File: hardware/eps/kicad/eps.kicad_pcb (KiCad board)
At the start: 2 copper layers, 96 x 90.2 mm, 85 parts, among them J1 B2B-PH-K-S(LF)(SN), J2 B2B-PH-K-S(LF)(SN), J3 B2B-PH-K-S(LF)(SN), J4 B2B-PH-K-S(LF)(SN), J5 B2B-PH-K-S(LF)(SN), J5 XT30PW-F, J6 B2B-PH-K-S(LF)(SN), J7 TSW-103-07-F-S, J8 68000-102HLF, J9 68000-102HLF, Q1 FDMC8327L, Q2 FDMC8327L, U1 LTC4162EUFD-LADMTRPBF, U2 TPS62933FDRLR, U3 TPS62933FDRLR

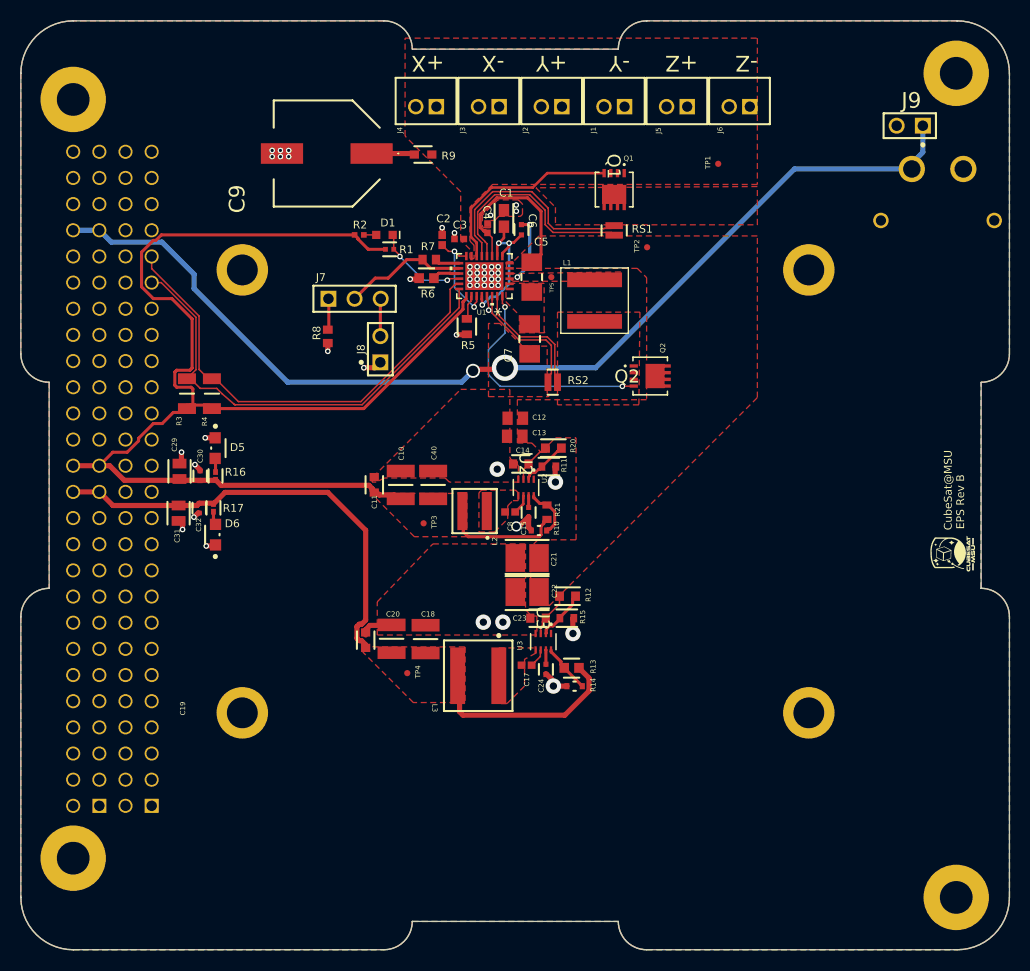
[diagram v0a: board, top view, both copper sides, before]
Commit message: attempt to convert altium to kicad, lost foot prints, not good
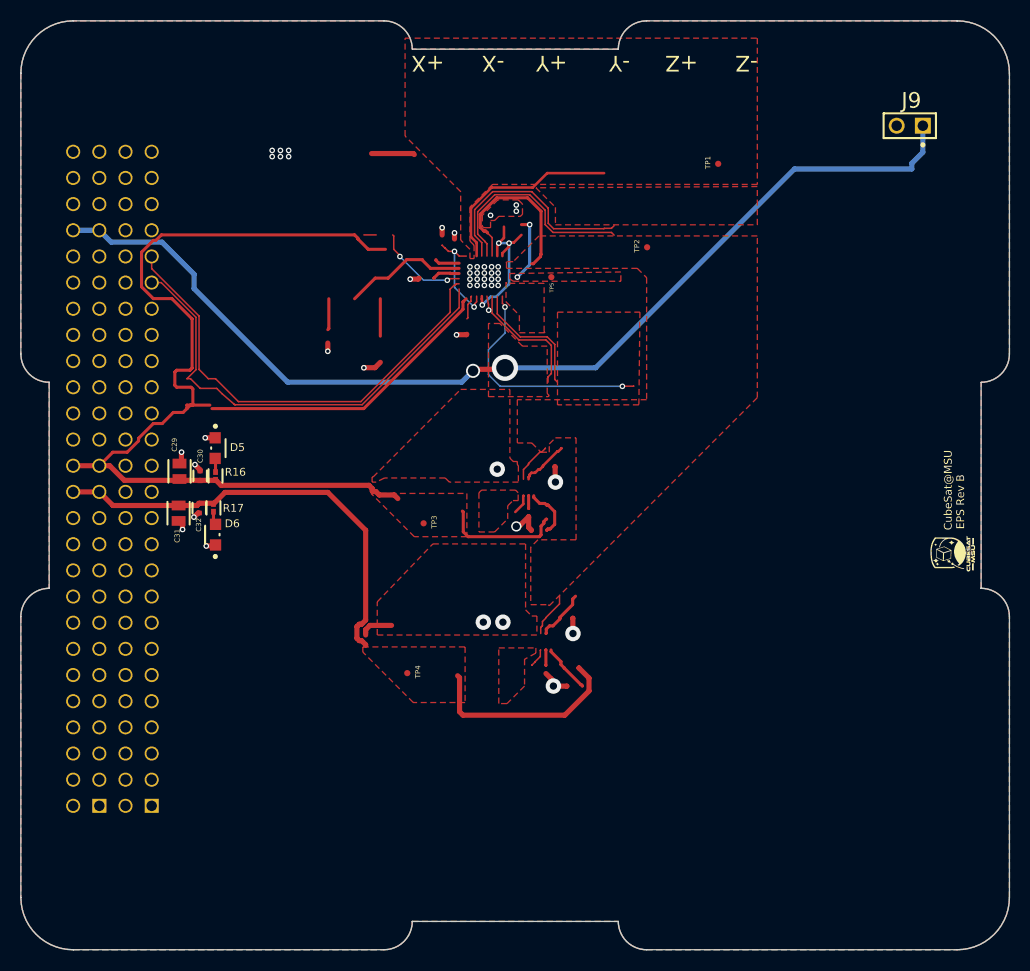
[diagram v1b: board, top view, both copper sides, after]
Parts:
- removed ? (x8): , 
- removed C1: GRM188R60J106ME47D, Vault:FP-GRM188-0_1-e0_2_0_55-IPC_A
- removed C10, C18, C19, C40: CL32A226KAJNNNE, SamacSys:CAPC3225X270N
- removed C11, C14, C20, C23: C14663, Vault:FP-CC0603-DA-MFG
- removed C12, C13: CL21B103KBANNNC, Vault:CAPC2013X75X45LL10T25
- removed C15: CC0402KRX7R9BB333, Vault:FP-CC0402-MFG
- removed C17, C8: CL05B104KO5NNNC, Vault:CAPC1050X55X23ML05T13
- removed C2: 0402YD105KAT2A, Vault:CAPC1005X56X25ML10T15
- removed C21, C22: GCM32EC7YA106KA03L, Vault:FP-GCM32E-0_3-IPC_B
- removed C24: CC0402KRX7R7BB333, Vault:FP-CC0402-MFG
- removed C3, C4: 04025C104KAT2A, SamacSys:CAPC1005X56N
- removed C5, C7: UMK316BBJ106KL-T, Vault:FP-1206-L_3_2_0_3-W_1_6_0-IPC_A
- removed C6: CC0402KRX7R8BB223, Vault:FP-CC0402-MFG
- removed C9: EEEFK1H151P, SamacSys:EEE0JA152UAP
- removed D1: 150060YS75000, Vault:WL-SMCW_0603_150060xx75000
- removed J1, J2, J3, J4, J5, J6: B2B-PH-K-S(LF)(SN), Vault:JST-B2B-PH-K-S_V
- removed J5: XT30PW-F, Vault:XT30PWF
- removed J7: TSW-103-07-F-S, Vault:SMTC-TSW-103-07-X-S
- removed J8: 68000-102HLF, Vault:AMPH-68000-102HLF_V
- removed L1: XAL6060-682MEC, SamacSys:XAL6060682MEC
- removed L2: 74438357047, Vault:WE-MAPI_4030
- removed L3: 74439346068, Vault:WE-XHMI_6060
- removed Q1, Q2: FDMC8327L, Vault:WDFN8_511DR_OSI
- removed R1: CRCW0402100KFKED, Vault:FP-CRCW0402-e3-IPC_C
- removed R10, R14: SG73P1JTTD1002F, Vault:FP-SG73P1J-MFG
- removed R11, R15: AC0603FR-0761K9L, Vault:FP-AC0603-IPC_C
- removed R12, R20: AC0603FR-07226KL, Vault:FP-AC0603-IPC_B
- removed R13: CRCW060352K3FKEA, Vault:FP-CRCW0603-e3-IPC_B
- removed R2: CRCW04022K20JNED, Vault:RESC1005X40X25NL05T05
- removed R21: RC0603FR-0731K6L, Vault:RESC1608X55X25NL10T15
- removed R3, R4: 1206W4F1002T5E, SamacSys:RESC3116X65N
- removed R5: CRCW060310K0JNEA, Vault:FP-CRCW0603-e3-MFG
- removed R6: CRCW060363K4FKEA, Vault:FP-CRCW0603-e3-IPC_B
- removed R7, R8: CRCW060310K0FKEA, Vault:RESC1609X50X30NL8T20
- removed R9: RT0603FRE072R49L, Vault:FP-RT0603-MFG
- removed RS1, RS2: PRL0816-R010-F-T1, Vault:FP-PRL0816-MFG
- removed U1: LTC4162EUFD-LADMTRPBF, Vault:05-08-1712_ADI
- removed U2, U3: TPS62933FDRLR, Vault:SOT5X3-8_DRL_TEX
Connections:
- net BATT_POS renamed /BATT_POS
- net NetD5_2 renamed Net-(D5-A)
- net NetD6_2 renamed Net-(D6-A)
- H1 pad 01: (no net) -> unconnected-(H1-Pad01)
- H1 pad 02: (no net) -> unconnected-(H1-Pad02)
- H1 pad 03: (no net) -> unconnected-(H1-Pad03)
- H1 pad 04: (no net) -> unconnected-(H1-Pad04)
- H1 pad 05: (no net) -> unconnected-(H1-Pad05)
- H1 pad 06: (no net) -> unconnected-(H1-Pad06)
- H1 pad 07: (no net) -> unconnected-(H1-Pad07)
- H1 pad 08: (no net) -> unconnected-(H1-Pad08)
- H1 pad 09: (no net) -> unconnected-(H1-Pad09)
- H1 pad 10: (no net) -> unconnected-(H1-Pad10)
- H1 pad 11: (no net) -> unconnected-(H1-Pad11)
- H1 pad 12: (no net) -> unconnected-(H1-Pad12)
- H1 pad 13: (no net) -> unconnected-(H1-Pad13)
- H1 pad 14: (no net) -> unconnected-(H1-Pad14)
- H1 pad 15: (no net) -> unconnected-(H1-Pad15)
- H1 pad 16: (no net) -> unconnected-(H1-Pad16)
- H1 pad 17: (no net) -> unconnected-(H1-Pad17)
- H1 pad 18: (no net) -> unconnected-(H1-Pad18)
- H1 pad 19: (no net) -> unconnected-(H1-Pad19)
- H1 pad 20: (no net) -> unconnected-(H1-Pad20)
- H1 pad 21: (no net) -> unconnected-(H1-Pad21)
- H1 pad 22: (no net) -> unconnected-(H1-Pad22)
- H1 pad 23: (no net) -> unconnected-(H1-Pad23)
- H1 pad 24: (no net) -> unconnected-(H1-Pad24)
- H1 pad 25: (no net) -> unconnected-(H1-Pad25)
- H1 pad 26: (no net) -> unconnected-(H1-Pad26)
- H1 pad 27: (no net) -> unconnected-(H1-Pad27)
- H1 pad 28: (no net) -> unconnected-(H1-Pad28)
- H1 pad 29: (no net) -> unconnected-(H1-Pad29)
- H1 pad 30: (no net) -> unconnected-(H1-Pad30)
- H1 pad 31: (no net) -> unconnected-(H1-Pad31)
- H1 pad 32: (no net) -> unconnected-(H1-Pad32)
- H1 pad 33: (no net) -> unconnected-(H1-Pad33)
- H1 pad 34: (no net) -> unconnected-(H1-Pad34)
- H1 pad 35: (no net) -> unconnected-(H1-Pad35)
- H1 pad 36: (no net) -> unconnected-(H1-Pad36)
- H1 pad 37: (no net) -> unconnected-(H1-Pad37)
- H1 pad 38: (no net) -> unconnected-(H1-Pad38)
- H1 pad 39: (no net) -> unconnected-(H1-Pad39)
- H1 pad 40: (no net) -> unconnected-(H1-Pad40)
- H1 pad 41: I2C_SDA -> /I2C_SDA
- H1 pad 42: (no net) -> unconnected-(H1-Pad42)
- H1 pad 43: I2C_SCL -> /I2C_SCL
- H1 pad 44: (no net) -> unconnected-(H1-Pad44)
- H1 pad 45: (no net) -> unconnected-(H1-Pad45)
- H1 pad 46: (no net) -> unconnected-(H1-Pad46)
- H1 pad 47: (no net) -> unconnected-(H1-Pad47)
- H1 pad 48: (no net) -> unconnected-(H1-Pad48)
- H1 pad 49: (no net) -> unconnected-(H1-Pad49)
- H1 pad 50: (no net) -> unconnected-(H1-Pad50)
- H1 pad 51: (no net) -> unconnected-(H1-Pad51)
- H1 pad 52: (no net) -> unconnected-(H1-Pad52)
- H2 pad 01: (no net) -> unconnected-(H2-Pad01)
- H2 pad 02: (no net) -> unconnected-(H2-Pad02)
- H2 pad 03: (no net) -> unconnected-(H2-Pad03)
- H2 pad 04: (no net) -> unconnected-(H2-Pad04)
- H2 pad 05: (no net) -> unconnected-(H2-Pad05)
- H2 pad 06: (no net) -> unconnected-(H2-Pad06)
- H2 pad 07: (no net) -> unconnected-(H2-Pad07)
- H2 pad 08: (no net) -> unconnected-(H2-Pad08)
- H2 pad 09: (no net) -> unconnected-(H2-Pad09)
- H2 pad 10: (no net) -> unconnected-(H2-Pad10)
- H2 pad 11: (no net) -> unconnected-(H2-Pad11)
- H2 pad 12: (no net) -> unconnected-(H2-Pad12)
- H2 pad 13: (no net) -> unconnected-(H2-Pad13)
- H2 pad 14: (no net) -> unconnected-(H2-Pad14)
- H2 pad 15: (no net) -> unconnected-(H2-Pad15)
- H2 pad 16: (no net) -> unconnected-(H2-Pad16)
- H2 pad 17: (no net) -> unconnected-(H2-Pad17)
- H2 pad 18: (no net) -> unconnected-(H2-Pad18)
- H2 pad 19: (no net) -> unconnected-(H2-Pad19)
- H2 pad 20: (no net) -> unconnected-(H2-Pad20)
- H2 pad 21: (no net) -> unconnected-(H2-Pad21)
- H2 pad 22: (no net) -> unconnected-(H2-Pad22)
- H2 pad 23: (no net) -> unconnected-(H2-Pad23)
- H2 pad 24: (no net) -> unconnected-(H2-Pad24)
- H2 pad 33: (no net) -> unconnected-(H2-Pad33)
- H2 pad 34: (no net) -> unconnected-(H2-Pad34)
- H2 pad 35: (no net) -> unconnected-(H2-Pad35)
- H2 pad 36: (no net) -> unconnected-(H2-Pad36)
- H2 pad 37: (no net) -> unconnected-(H2-Pad37)
- H2 pad 38: (no net) -> unconnected-(H2-Pad38)
- H2 pad 39: (no net) -> unconnected-(H2-Pad39)
- H2 pad 40: (no net) -> unconnected-(H2-Pad40)
- H2 pad 41: (no net) -> unconnected-(H2-Pad41)
- H2 pad 42: (no net) -> unconnected-(H2-Pad42)
- H2 pad 43: (no net) -> unconnected-(H2-Pad43)
- H2 pad 44: (no net) -> unconnected-(H2-Pad44)
- H2 pad 47: (no net) -> unconnected-(H2-Pad47)
- H2 pad 48: (no net) -> unconnected-(H2-Pad48)
- H2 pad 49: (no net) -> unconnected-(H2-Pad49)
- H2 pad 50: (no net) -> unconnected-(H2-Pad50)
- H2 pad 51: (no net) -> unconnected-(H2-Pad51)
- H2 pad 52: (no net) -> unconnected-(H2-Pad52)
- TP1 pad 1: VIN_CHG -> /VIN_CHG
- TP2 pad 1: VOUT_PP -> /VOUT_PP
- TP5 pad 1: SW_NODE -> /SW_NODE
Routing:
- net (no net): track 0.00 -> 229.0 mm, vias 0 -> 10
- net VOUT_PP: track 46.7 -> 0.00 mm
- net I2C_SCL: track 45.5 -> 0.00 mm
- net /I2C_SCL: track 0.00 -> 45.5 mm
- net I2C_SDA: track 45.2 -> 0.00 mm
- net /I2C_SDA: track 0.00 -> 45.2 mm
- net NetQ2_4: track 23.0 -> 0.00 mm, vias 2 -> 0
- net NetQ1_5: track 21.5 -> 0.00 mm
- net NetQ1_4: track 19.2 -> 0.00 mm
- net INTVcc: track 15.5 -> 0.00 mm, vias 3 -> 0
- net /BATT_POS: track 115.0 -> 101.2 mm, vias 3 -> 2
- net NetL1_2: track 12.3 -> 0.00 mm
- net NetJ7_2: track 12.0 -> 0.00 mm
- net NetC2_2: track 10.2 -> 0.00 mm, vias 2 -> 0
- net SMBALERT_N: track 9.15 -> 0.00 mm, vias 2 -> 0
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- added copper zone on F.Cu, net (none)
- added copper zone on F.Cu, net /SW_NODE
- added copper zone on F.Cu, net /VIN_CHG
- added copper zone on F.Cu, net /VOUT_PP
- removed copper zone on F.Cu, net NetC17_2
- removed copper zone on F.Cu, net NetC8_2
- removed copper zone on F.Cu, net NetL1_2
- removed copper zone on F.Cu, net NetQ1_5
- removed copper zone on F.Cu, net SW_NODE
- removed copper zone on F.Cu, net VIN_CHG
- removed copper zone on F.Cu, net VOUT_PP

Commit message: eps/kicad: assemble the schematic hierarchy and link it to the PCB
  The three .kicad_sch files were independent roots from the Altium import.
  Opening the project showed only the root's 17 components; the other 60
  were in files KiCad had no path to. Separately, the PCB shared no UUIDs
  at all with any schematic -- it had been imported independently, so the
  board-to-schematic link did not exist rather than being broken.

  Both are now fixed. Root sheet carries sheet symbols for Regulation and
  Solar_Charger, and all 77 footprints link to their symbols: 17 on the
  root, 28 in Regulation, 32 in Solar_Charger, matching the schematics
  exactly. Sheet-local nets picked up hierarchical paths, which cleared
  the "via connected to unknown net" warnings.

  Getting there took several passes and two things had to be repaired
  first.

  Annotation. Building the hierarchy in KiCad re-annotated the child
  sheets -- Solar_Charger went J1-J8 to J11-J18, C1-C24 became C41-C52 --
  because a duplicate J5 blocked the assembly. The refdes are the only
  link to the board, so 69 footprints were deleted as orphans. Every
  symbol UUID survived, so the old annotation was restored exactly by
  UUID, and the board was restored from the previous commit. The J5
  collision is resolved properly: J5 is the JST connector, and the XT30
  that shared its designator is now J10, on both the schematic and the
  board.

  Footprint fields. The import left them unusable -- only 5 of 40 carried
  a library prefix, and 10 pointed at
  C__Users_dng_Documents_AltiumLL_SamacSys.PcbLib, a Windows path from the
  machine that ran the import. All 77 are now the board's own qualified
  ids, which removed about 60 "missing a library name" warnings per
  update.

  The last 11 footprints would not link no matter how the update dialog
  was configured: KiCad matched 66 by UUID path and never fell back to
  reference designators for the remainder. Their paths were written
  directly instead, following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
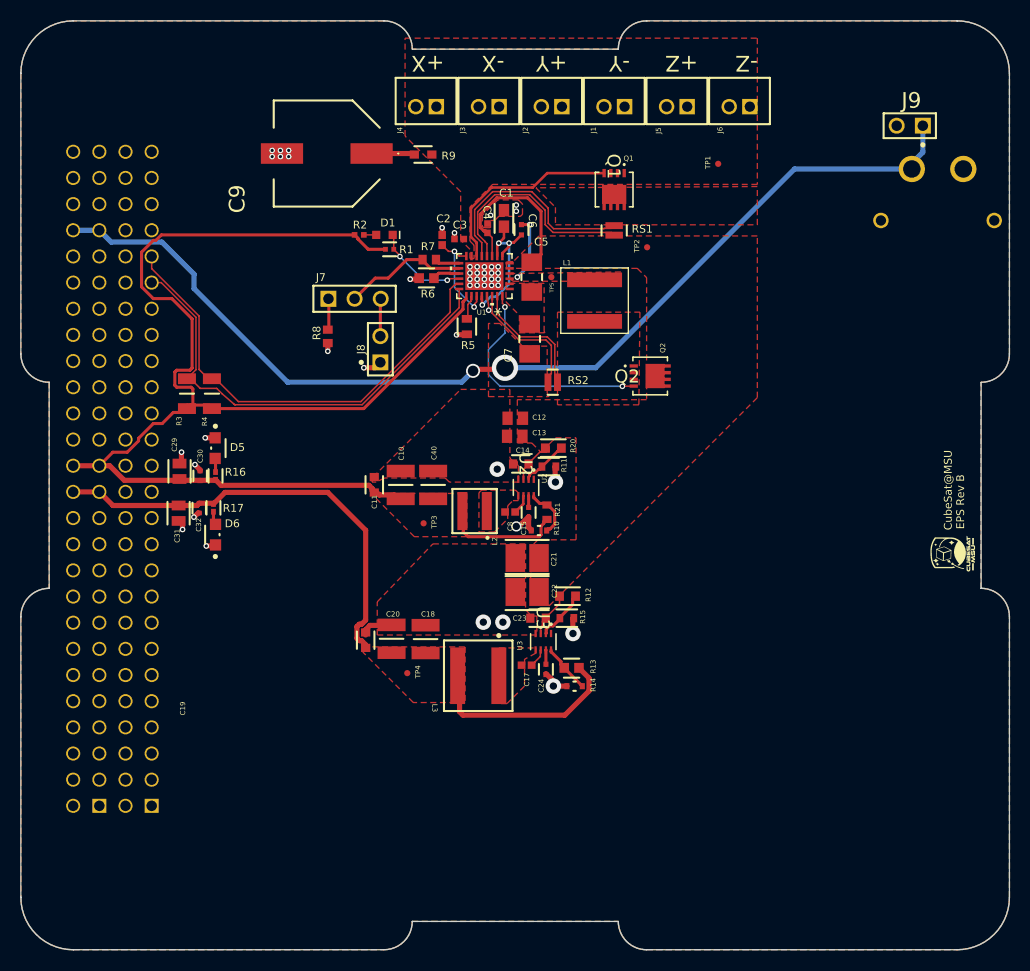
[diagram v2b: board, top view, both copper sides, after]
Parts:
- added C1: GRM188R60J106ME47D, Vault:FP-GRM188-0_1-e0_2_0_55-IPC_A, F.Cu at (147.4, 79.1)
- added C10: CL32A226KAJNNNE, SamacSys:CAPC3225X270N, F.Cu at (137.4, 105.0)
- added C11: C14663, Vault:FP-CC0603-DA-MFG, F.Cu at (134.8, 105.0)
- added C12: CL21B103KBANNNC, Vault:CAPC2013X75X45LL10T25, F.Cu at (148.5, 98.5)
- added C13: CL21B103KBANNNC, Vault:CAPC2013X75X45LL10T25, F.Cu at (148.5, 100.2)
- added C14: C14663, Vault:FP-CC0603-DA-MFG, F.Cu at (149.0, 102.9)
- added C15: CC0402KRX7R9BB333, Vault:FP-CC0402-MFG, F.Cu at (149.8, 107.6)
- added C17: CL05B104KO5NNNC, Vault:CAPC1050X55X23ML05T13, F.Cu at (149.6, 122.5)
- added C18: CL32A226KAJNNNE, SamacSys:CAPC3225X270N, F.Cu at (139.8, 119.9)
- added C19: CL32A226KAJNNNE, SamacSys:CAPC3225X270N, F.Cu at (136.5, 119.9)
- added C2: 0402YD105KAT2A, Vault:CAPC1005X56X25ML10T15, F.Cu at (141.4, 81.2)
- added C20: C14663, Vault:FP-CC0603-DA-MFG, F.Cu at (134.0, 120.0)
- added C21: GCM32EC7YA106KA03L, Vault:FP-GCM32E-0_3-IPC_B, F.Cu at (149.7, 112.1)
- added C22: GCM32EC7YA106KA03L, Vault:FP-GCM32E-0_3-IPC_B, F.Cu at (149.7, 115.4)
- added C23: C14663, Vault:FP-CC0603-DA-MFG, F.Cu at (150.7, 117.9)
- added C24: CC0402KRX7R7BB333, Vault:FP-CC0402-MFG, F.Cu at (151.5, 122.9)
- added C3: 04025C104KAT2A, SamacSys:CAPC1005X56N, F.Cu at (143.1, 81.1)
- added C4: 04025C104KAT2A, SamacSys:CAPC1005X56N, F.Cu at (145.8, 80.0)
- added C40: CL32A226KAJNNNE, SamacSys:CAPC3225X270N, F.Cu at (140.5, 105.0)
- added C5: UMK316BBJ106KL-T, Vault:FP-1206-L_3_2_0_3-W_1_6_0-IPC_A, F.Cu at (150.1, 84.8)
- added C6: CC0402KRX7R8BB223, Vault:FP-CC0402-MFG, F.Cu at (149.1, 80.2)
- added C7: UMK316BBJ106KL-T, Vault:FP-1206-L_3_2_0_3-W_1_6_0-IPC_A, F.Cu at (149.9, 90.8)
- added C8: CL05B104KO5NNNC, Vault:CAPC1050X55X23ML05T13, F.Cu at (148.0, 107.6)
- added C9: EEEFK1H151P, SamacSys:EEE0JA152UAP, F.Cu at (130.2, 72.8)
- added D1: 150060YS75000, Vault:WL-SMCW_0603_150060xx75000, F.Cu at (135.8, 80.7)
- added J1: B2B-PH-K-S(LF)(SN), Vault:JST-B2B-PH-K-S_V, F.Cu at (158.1, 67.7)
- added J10: XT30PW-F, Vault:XT30PWF, B.Cu at (187.0, 74.3)
- added J2: B2B-PH-K-S(LF)(SN), Vault:JST-B2B-PH-K-S_V, F.Cu at (152.0, 67.7)
- added J3: B2B-PH-K-S(LF)(SN), Vault:JST-B2B-PH-K-S_V, F.Cu at (145.9, 67.7)
- added J4: B2B-PH-K-S(LF)(SN), Vault:JST-B2B-PH-K-S_V, F.Cu at (139.9, 67.7)
- added J5: B2B-PH-K-S(LF)(SN), Vault:JST-B2B-PH-K-S_V, F.Cu at (164.2, 67.7)
- added J6: B2B-PH-K-S(LF)(SN), Vault:JST-B2B-PH-K-S_V, F.Cu at (170.3, 67.7)
- added J7: TSW-103-07-F-S, Vault:SMTC-TSW-103-07-X-S, F.Cu at (130.4, 86.9)
- added J8: 68000-102HLF, Vault:AMPH-68000-102HLF_V, F.Cu at (135.4, 91.8)
- added L1: XAL6060-682MEC, SamacSys:XAL6060682MEC, F.Cu at (156.2, 87.1)
- added L2: 74438357047, Vault:WE-MAPI_4030, F.Cu at (144.6, 107.5)
- added L3: 74439346068, Vault:WE-XHMI_6060, F.Cu at (144.9, 123.5)
- added Q1: FDMC8327L, Vault:WDFN8_511DR_OSI, F.Cu at (158.1, 76.3)
- added Q2: FDMC8327L, Vault:WDFN8_511DR_OSI, F.Cu at (161.6, 94.4)
- added R1: CRCW0402100KFKED, Vault:FP-CRCW0402-e3-IPC_C, F.Cu at (136.3, 82.1)
- added R10: SG73P1JTTD1002F, Vault:FP-SG73P1J-MFG, F.Cu at (150.8, 109.4)
- added R11: AC0603FR-0761K9L, Vault:FP-AC0603-IPC_C, F.Cu at (151.8, 103.2)
- added R12: AC0603FR-07226KL, Vault:FP-AC0603-IPC_B, F.Cu at (153.6, 115.8)
- added R13: CRCW060352K3FKEA, Vault:FP-CRCW0603-e3-IPC_B, F.Cu at (154.0, 122.7)
- added R14: SG73P1JTTD1002F, Vault:FP-SG73P1J-MFG, F.Cu at (154.3, 124.5)
- added R15: AC0603FR-0761K9L, Vault:FP-AC0603-IPC_C, F.Cu at (153.5, 117.9)
- added R2: CRCW04022K20JNED, Vault:RESC1005X40X25NL05T05, F.Cu at (133.4, 80.7)
- added R20: AC0603FR-07226KL, Vault:FP-AC0603-IPC_B, F.Cu at (152.2, 101.4)
- added R21: RC0603FR-0731K6L, Vault:RESC1608X55X25NL10T15, F.Cu at (151.6, 107.6)
- added R3: 1206W4F1002T5E, SamacSys:RESC3116X65N, F.Cu at (116.6, 96.1)
- added R4: 1206W4F1002T5E, SamacSys:RESC3116X65N, F.Cu at (119.1, 96.1)
- added R5: CRCW060310K0JNEA, Vault:FP-CRCW0603-e3-MFG, F.Cu at (143.8, 89.6)
- added R6: CRCW060363K4FKEA, Vault:FP-CRCW0603-e3-IPC_B, F.Cu at (139.9, 84.9)
- added R7: CRCW060310K0FKEA, Vault:RESC1609X50X30NL8T20, F.Cu at (140.2, 83.1)
- added R8: CRCW060310K0FKEA, Vault:RESC1609X50X30NL8T20, F.Cu at (130.3, 90.5)
- added R9: RT0603FRE072R49L, Vault:FP-RT0603-MFG, F.Cu at (139.6, 72.9)
- added RS1: PRL0816-R010-F-T1, Vault:FP-PRL0816-MFG, F.Cu at (158.1, 80.3)
- added RS2: PRL0816-R010-F-T1, Vault:FP-PRL0816-MFG, F.Cu at (152.2, 95.0)
- added U1: LTC4162EUFD-LADMTRPBF, Vault:05-08-1712_ADI, F.Cu at (145.5, 84.7)
- added U2: TPS62933FDRLR, Vault:SOT5X3-8_DRL_TEX, F.Cu at (149.6, 105.2)
- added U3: TPS62933FDRLR, Vault:SOT5X3-8_DRL_TEX, F.Cu at (151.2, 120.2)
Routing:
- net (no net): track 229.0 -> 90.6 mm, vias 10 -> 0
- net /I2C_SCL: track 45.5 -> 0.00 mm
- net /I2C_SDA: track 45.2 -> 0.00 mm
- net /Solar_Charger/VOUT_PP: track 0.00 -> 38.3 mm
- net Net-(U1-BATFET): track 0.00 -> 23.0 mm, vias 0 -> 2
- net Net-(U1-CLP): track 0.00 -> 21.5 mm
- net Net-(U1-INFET): track 0.00 -> 19.2 mm
- net /Solar_Charger/INTVcc: track 0.00 -> 15.5 mm, vias 0 -> 3
- net /Solar_Charger/BATT_POS: track 0.00 -> 13.8 mm, vias 0 -> 1
- net Net-(U1-CSP): track 0.00 -> 12.3 mm
- net Net-(U1-NTC): track 0.00 -> 12.0 mm
- net Net-(U1-CELLS0): track 0.00 -> 10.2 mm, vias 0 -> 2
- net /Solar_Charger/SMBALERT_N: track 0.00 -> 9.15 mm, vias 0 -> 2
- net /Regulation/VOUT_PP: track 0.00 -> 8.34 mm
- net /Solar_Charger/SW_NODE: track 0.00 -> 6.40 mm, vias 0 -> 2
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- added copper zone on F.Cu, net /Solar_Charger/BATT_POS
- added copper zone on F.Cu, net /Solar_Charger/SW_NODE
- added copper zone on F.Cu, net Net-(U1-CLP)
- added copper zone on F.Cu, net Net-(U1-CSP)
- added copper zone on F.Cu, net Net-(U2-SW)
- added copper zone on F.Cu, net Net-(U3-SW)
- removed copper zone on F.Cu, net (none)
- removed copper zone on F.Cu, net /BATT_POS
- removed copper zone on F.Cu, net /SW_NODE
